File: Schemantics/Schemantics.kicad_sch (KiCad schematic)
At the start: 23 parts, among them IC1 MCP73831T-2ACI_OT, IC2 MCP1725-3302E_MC, J1 Conn_01x04, J2 Conn_01x02, Q1 BC547, U1 ESP32-WROOM-32D

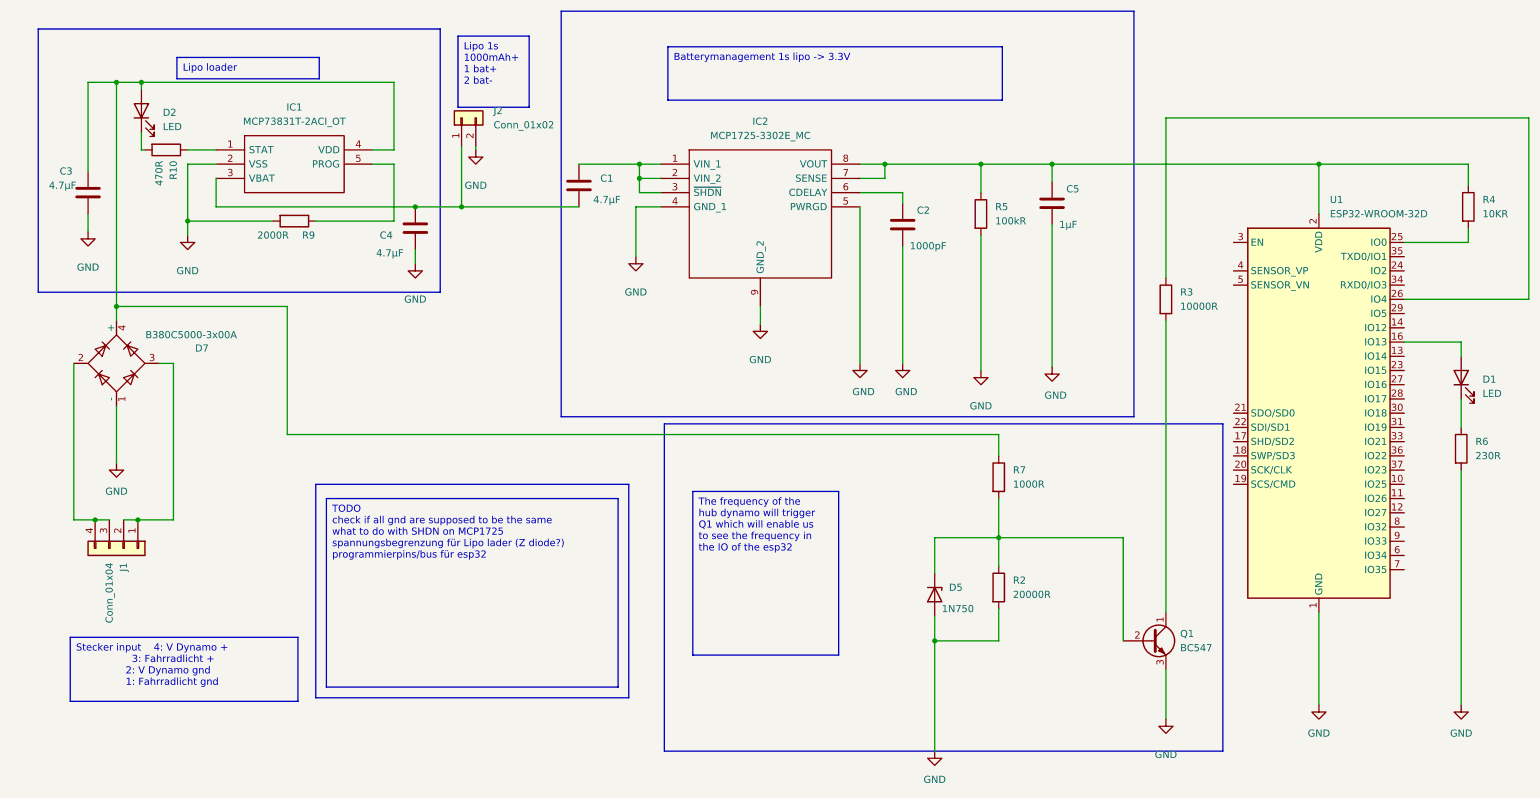
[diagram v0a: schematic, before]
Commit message: rework for better visability, added net labels
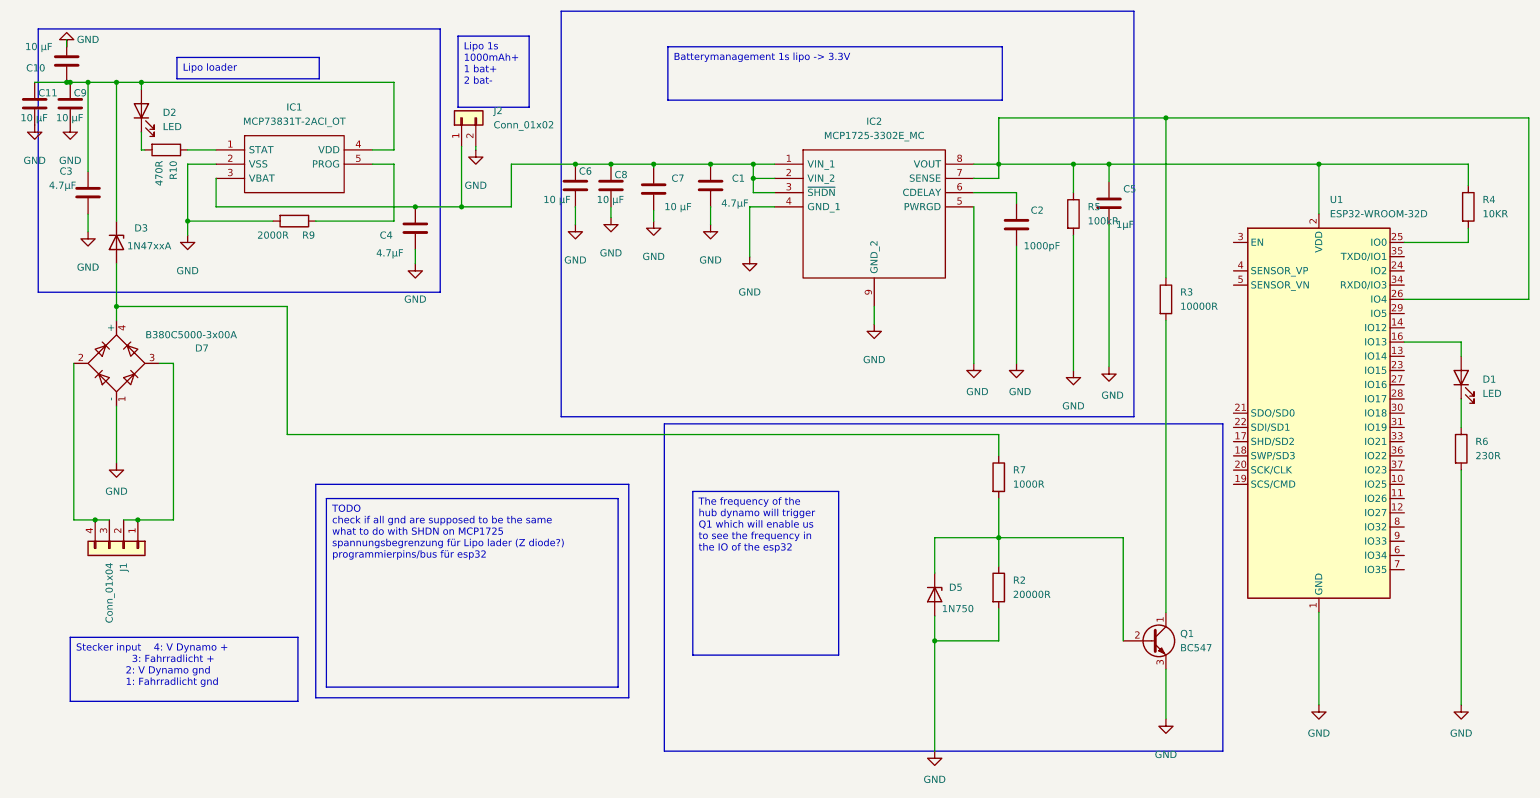
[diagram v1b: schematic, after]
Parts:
- added C10, C11, C6, C7, C8, C9: 10 μF, Capacitor_THT:C_Rect_L16.5mm_W4.7mm_P15.00mm_MKT, symbol Device:C
- added D3: 1N47xxA, Diode_THT:D_DO-41_SOD81_P10.16mm_Horizontal, symbol Diode:1N47xxA
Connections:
- net GND: now also C1.2, C10.2, C11.2, C6.2, C7.2, C8.2, C9.2
- net at C4.1, IC1.3 (VBAT), J2.1 (Pin_1): now also C1.1, IC2.1 (VIN_1), IC2.2 (VIN_2), IC2.3 (~{SHDN}), C6.1, C7.1, C8.1; no longer C1.2
- net at C3.1, D2.2 (A), IC1.4 (VDD): now also C10.1, C11.1, C9.1, D3.1 (K); no longer D7.4 (+), R7.1
- net at C5.1, IC2.7 (SENSE), IC2.8 (VOUT)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: now also R3.1, U1.26 (IO4)
- new net: D3.2 (A), D7.4 (+), R7.1
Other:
- moved on the sheet: C1, C2, C5, IC2, R5
